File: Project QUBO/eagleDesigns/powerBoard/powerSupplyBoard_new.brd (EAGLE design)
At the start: 152.4 x 101.6 mm, 146 parts

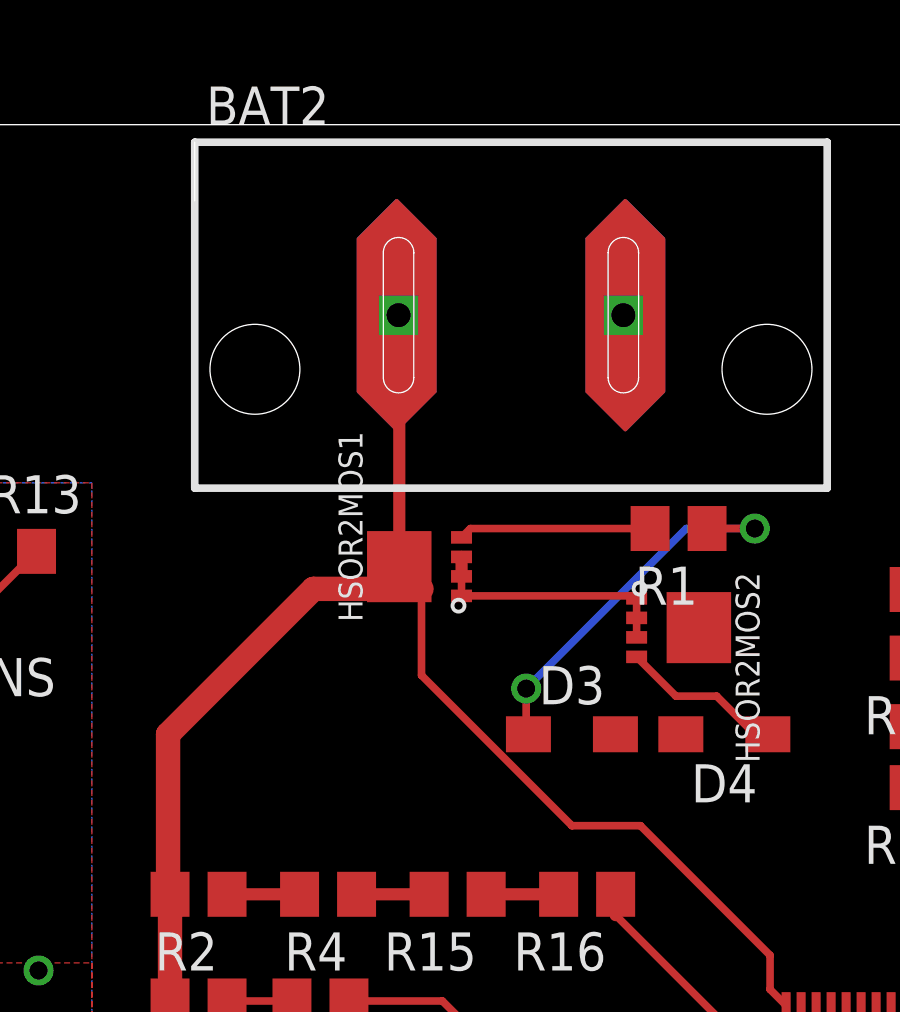
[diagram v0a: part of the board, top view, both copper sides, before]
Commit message: 
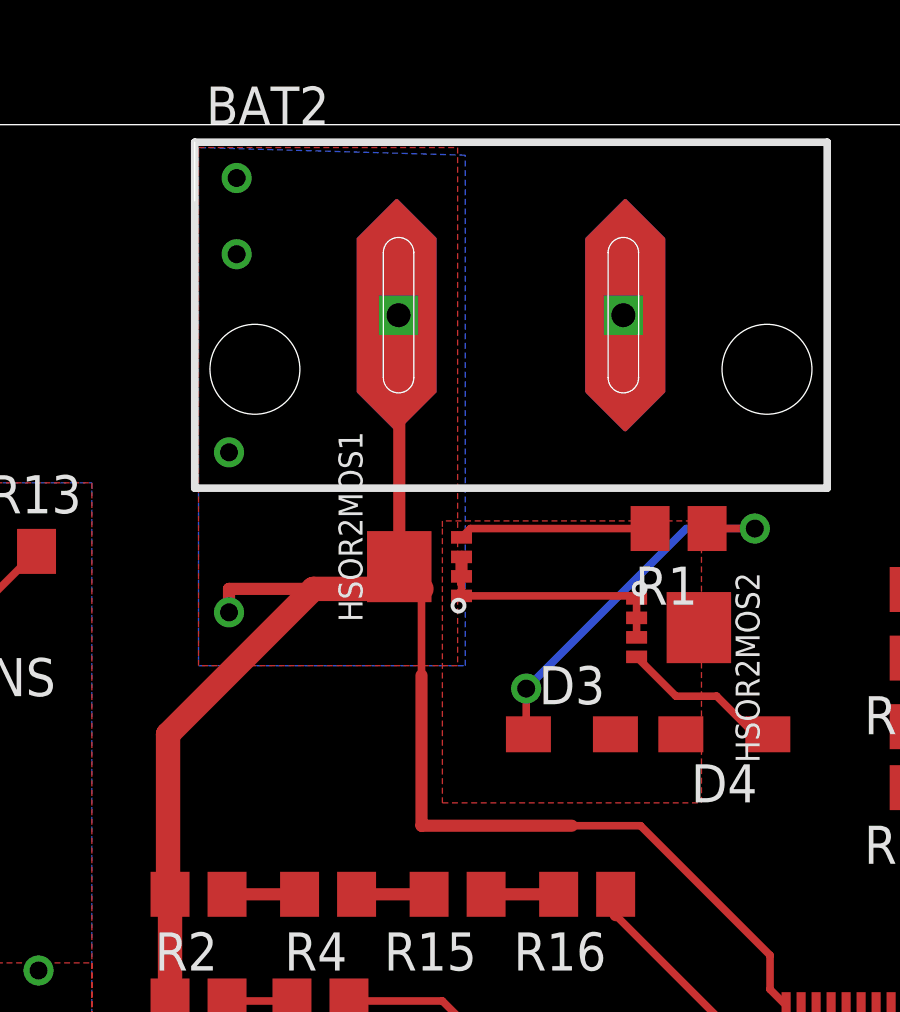
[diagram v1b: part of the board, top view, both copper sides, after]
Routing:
- net BAT2: track 52.9 -> 59.4 mm, vias 0 -> 4
- added copper zone on layer 1, net BAT2
- added copper zone on layer 16, net BAT2
- added copper zone on layer 1, net N$27
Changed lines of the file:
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@@
 <wire x1="67.31" y1="81.28" x2="67.31" y2="76.012" width="0.8128" layer="1"/>
 <wire x1="67.31" y1="76.012" x2="67.376" y2="75.946" width="0.254" layer="1"/>
-<wire x1="75.758" y1="86.127" x2="75.758" y2="83.246" width="0.254" layer="1"/>
-<wire x1="75.758" y1="83.246" x2="80.772" y2="78.232" width="0.254" layer="1"/>
-<wire x1="80.772" y1="78.232" x2="83.058" y2="78.232" width="0.254" layer="1"/>
+<wire x1="75.758" y1="83.246" x2="75.758" y2="86.127" width="0.254" layer="1"/>
+<wire x1="83.058" y1="78.232" x2="80.772" y2="78.232" width="0.254" layer="1"/>
 <wire x1="83.058" y1="78.232" x2="87.376" y2="73.914" width="0.254" layer="1"/>
 <wire x1="87.376" y1="73.914" x2="87.376" y2="72.776" width="0.254" layer="1"/>
 <wire x1="87.376" y1="72.776" x2="87.912" y2="72.24" width="0.254" layer="1"/>
+<wire x1="80.772" y1="78.232" x2="75.758" y2="78.232" width="0.4064" layer="1"/>
+<wire x1="75.758" y1="78.232" x2="75.758" y2="83.246" width="0.4064" layer="1"/>
+<polygon width="0.4064" layer="1">
+<vertex x="68.326" y="100.838"/>
+<vertex x="76.962" y="100.838"/>
+<vertex x="76.962" y="83.566"/>
+<vertex x="68.326" y="83.566"/>
+<vertex x="68.326" y="100.584"/>
+</polygon>
+<polygon width="0.4064" layer="16">
+<vertex x="68.326" y="100.838"/>
+<vertex x="68.326" y="83.566"/>
+<vertex x="77.216" y="83.566"/>
+<vertex x="77.216" y="100.584"/>
+<vertex x="68.326" y="100.838"/>
+</polygon>
+<via x="69.596" y="99.822" extent="1-16" drill="0.6"/>
+<via x="69.596" y="97.282" extent="1-16" drill="0.6"/>
+<via x="69.342" y="90.678" extent="1-16" drill="0.6"/>
+<via x="69.342" y="85.344" extent="1-16" drill="0.6"/>
+<wire x1="72.157" y1="86.127" x2="69.342" y2="86.127" width="0.4064" layer="1"/>
+<wire x1="69.342" y1="86.127" x2="69.342" y2="85.344" width="0.4064" layer="1"/>
 <wire x1="87.912" y1="72.24" x2="146.37" y2="64.77" width="0" layer="19" extent="1-1"/>
 </signal>
@@
 <wire x1="77.092" y1="85.893" x2="82.846" y2="85.893" width="0.254" layer="1"/>
 <wire x1="82.846" y1="85.893" x2="82.928" y2="85.811" width="0.254" layer="1"/>
-<wire x1="82.222" y1="81.28" x2="84.402" y2="81.28" width="0" layer="19" extent="1-1"/>
-<wire x1="82.928" y1="84.511" x2="82.222" y2="81.28" width="0" layer="19" extent="1-1"/>
-<wire x1="89.412" y1="72.24" x2="84.402" y2="81.28" width="0" layer="19" extent="1-1"/>
+<polygon width="0.4064" layer="1" rank="2">
+<vertex x="76.454" y="88.138"/>
+<vertex x="76.454" y="78.994"/>
+<vertex x="85.09" y="78.994"/>
+<vertex x="85.09" y="88.392"/>
+<vertex x="76.454" y="88.392"/>
+</polygon>
+<wire x1="84.402" y1="81.28" x2="89.412" y2="72.24" width="0" layer="19" extent="1-1"/>
 </signal>
 <signal name="N$29">

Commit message: 
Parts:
- moved BAT2CS 25.5 mm to (104.6, 65.5), turned to 270 degrees
- moved R17 0.25 mm to (87.1, 61.0)
- moved R22 0.25 mm to (93.0, 79.2), turned to 0 degrees
- turned R20 to 180 degrees
- turned R21 to 0 degrees
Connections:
- new net UWEEN: DVL_12VREG.ONOFF, IOEXPANDER.9
- net BAT1: now also BAT1.P$2
- net BAT2: now also BAT2.P$2
- net BAT3: now also SHORE.P$2
- net GND: no longer BAT1.P$2, BAT2.P$2, SHORE.P$2
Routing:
- net BAT2HSOROUT: track 0.00 -> 25.4 mm, vias 0 -> 2
- net N$5: track 0.00 -> 22.2 mm
- net N$23: track 0.00 -> 15.1 mm
- net N$2: track 13.0 -> 27.2 mm
- net N$27: track 8.47 -> 19.6 mm
- net N$4: track 5.44 -> 15.6 mm
- net N$34: track 0.00 -> 3.38 mm
- net N$22: track 0.00 -> 2.29 mm
- net GND: track 167.5 -> 165.8 mm
- net BAT3HSOROUT: track 55.7 -> 55.9 mm, vias 4 -> 9

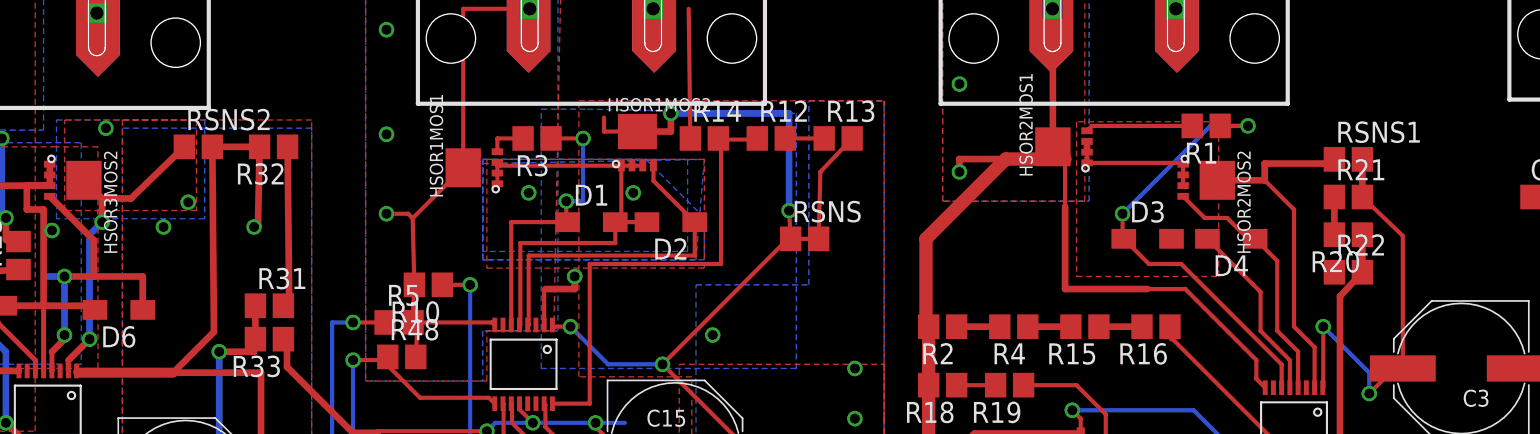
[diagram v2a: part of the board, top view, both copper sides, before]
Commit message: got rid of sense resistor on psb
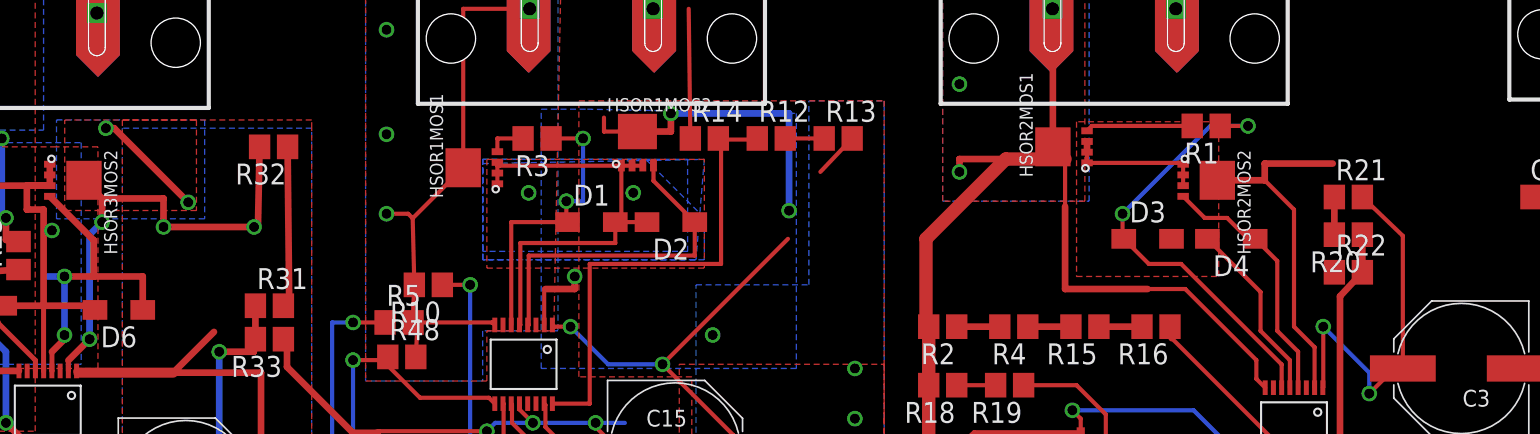
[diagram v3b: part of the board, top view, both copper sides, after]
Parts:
- removed RSNS, RSNS1, RSNS2: 2 mO, resistor:R0805
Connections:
- removed net N$1: BAT1HSOR.SENSE, HSOR1MOS2.DRAIN, RSNS.1
- removed net N$43: BAT3HSOR.SENSE, HSOR3MOS2.DRAIN, RSNS2.1
- removed net N$5: BAT2HSOR.SENSE, HSOR2MOS2.DRAIN, RSNS1.1
- net BAT1HSOROUT: now also BAT1HSOR.SENSE, HSOR1MOS2.DRAIN; no longer RSNS.2
- net BAT2HSOROUT: now also BAT2HSOR.SENSE, HSOR2MOS2.DRAIN; no longer RSNS1.2
- net BAT3HSOROUT: now also BAT3HSOR.SENSE, HSOR3MOS2.DRAIN; no longer RSNS2.2
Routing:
- net N$1: track 25.7 -> 0.00 mm, vias 3 -> 0
- net N$5: track 22.2 -> 0.00 mm
- net BAT2HSOROUT: track 25.4 -> 44.9 mm
- net BAT1HSOROUT: track 44.3 -> 62.4 mm, vias 6 -> 9
- net N$43: track 19.2 -> 6.86 mm, vias 4 -> 2
- net BAT3HSOROUT: track 55.9 -> 65.7 mm, vias 9 -> 11

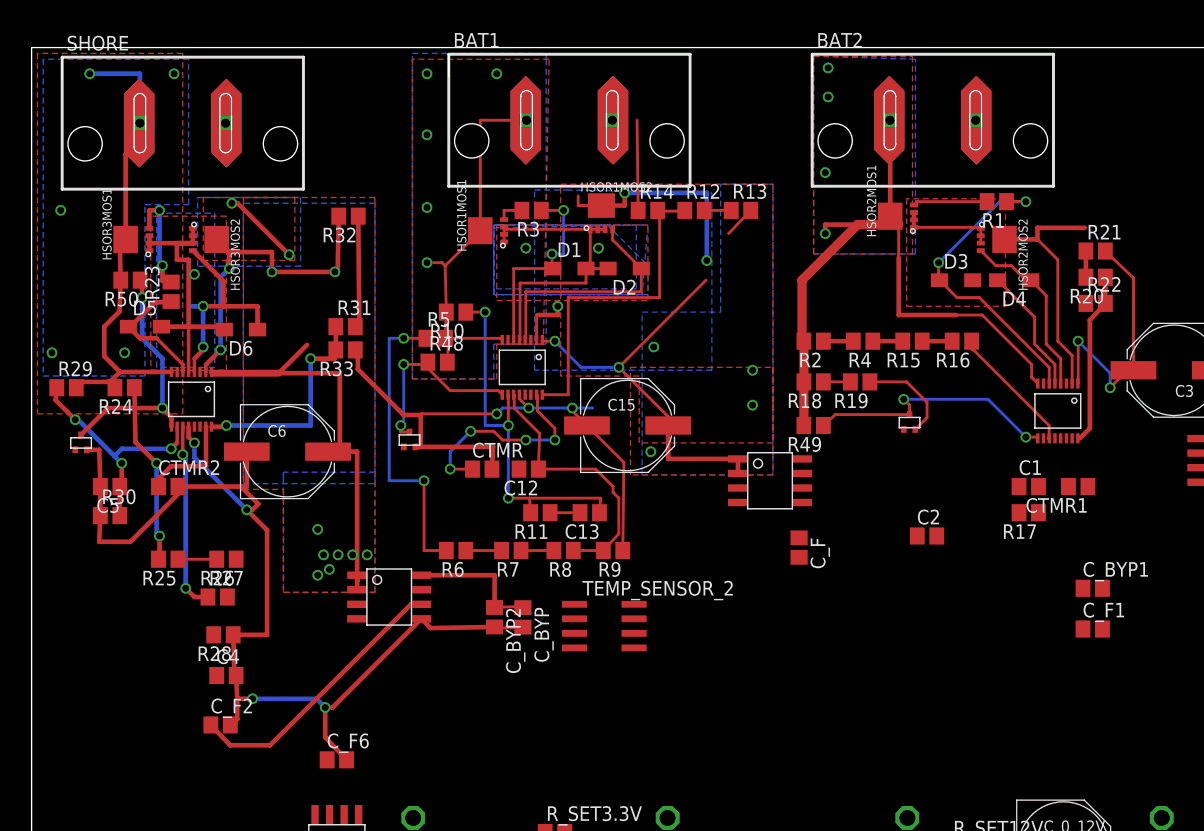
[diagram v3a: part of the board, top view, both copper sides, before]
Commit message: 
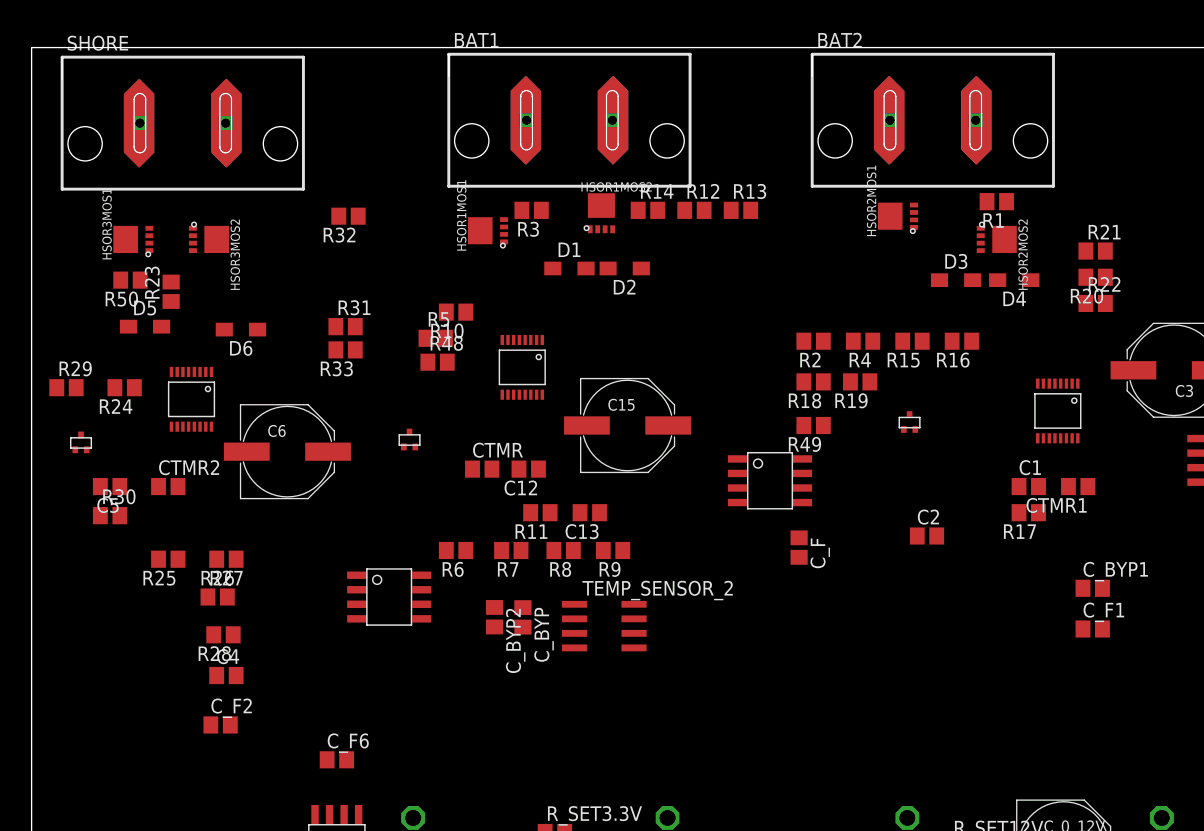
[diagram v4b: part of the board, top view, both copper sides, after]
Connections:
- removed net GND: 12VCS.P$5, 12VREG.P$1, 12VREG.P$2, 16VCS.P$5, 16V_CON.P$1, 3.3VCS.P$5, 3.3VREG.P$1, 3.3VREG.P$2, 5VCS.P$5, 5VREG.AGND1, 5VREG.AGND2, 5VREG.PGND, 5VREG.SYNC, ADC.COM, ADC.F0, ADC.GND0, ADC.GND1, ADC.GND2, ADC.GND3, ADC.GND4, ADC.GND5, ADC.GND6, ADC.REF-, BAT1CS.P$5, BAT1HSOR.GND, BAT2CS.P$5, BAT2HSOR.GND, BAT3CS.P$5, BAT3HSOR.GND, C1.2, C12.2, C15.-, C2.2, C3.-, C4.2, C5.2, C6.-, CTMR.2, CTMR1.2, CTMR2.2, C_0_12V.-, C_0_3.3V.-, C_1_12V.2, C_1_3.3V.2, C_BYP.2, C_BYP1.2, C_BYP2.2, C_BYP3.2, C_BYP4.2, C_BYP5.2, C_BYP6.2, C_BYP7.2, C_F.2, C_F1.2, C_F2.2, C_F3.2, C_F4.2, C_F5.2, C_F6.2, C_IN_5V.2, C_OUT_5V.-, DVL_12VREG.-VIN, HIGHSIDEMOS1.S, HIGHSIDEMOS2.S, HIGHSIDEMOS3.S, IOEXPANDER.12, JP1.12, JP1.15, JP1.18, JP1.24, JP1.33, JP1.34, JP1.37, JP1.39, JP1.4, JP1.40, JP1.44, JP1.64, R14.1, R17.1, R19.1, R22.1, R28.1, R30.1, R33.1, R35.1, R37.1, R39.1, R41.1, R43.1, R45.1, R47.1, R9.1, REN_B.1, REN_B.2, REN_H.1, REN_T.2, RFBB.2, R_LOAD.1, R_SET12V.1, R_SET3.3V.1, TEMP_SENSOR_1.4, TEMP_SENSOR_2.4, U$10.GND, U$14.S, U$15.S, U$16.GND, U$17.VCC, U$18.GND, U$5.A, U$5.C, U$6.GND, U$9.GND
- removed net N$100: JP1.36
- removed net SCL1: ADC.SCL, IOEXPANDER.22, JP1.10
- removed net SDA1: ADC.SDA, IOEXPANDER.23, JP1.9
- new net AGND: 12VCS.P$5, 12VREG.P$1, 12VREG.P$2, 16VCS.P$5, 16V_CON.P$1, 3.3VCS.P$5, 3.3VREG.P$1, 3.3VREG.P$2, 5VCS.P$5, 5VREG.AGND1, 5VREG.AGND2, 5VREG.PGND, 5VREG.SYNC, ADC.F0, BAT1CS.P$5, BAT1HSOR.GND, BAT2CS.P$5, BAT2HSOR.GND, BAT3CS.P$5, BAT3HSOR.GND, C1.2, C12.2, C15.-, C2.2, C3.-, C4.2, C5.2, C6.-, CTMR.2, CTMR1.2, CTMR2.2, C_0_12V.-, C_0_3.3V.-, C_1_12V.2, C_1_3.3V.2, C_BYP.2, C_BYP1.2, C_BYP2.2, C_BYP3.2, C_BYP4.2, C_BYP5.2, C_BYP6.2, C_BYP7.2, C_F.2, C_F1.2, C_F2.2, C_F3.2, C_F4.2, C_F5.2, C_F6.2, C_IN_5V.2, C_OUT_5V.-, DVL_12VREG.-VIN, HIGHSIDEMOS1.S, HIGHSIDEMOS2.S, HIGHSIDEMOS3.S, JP1.19, JP1.20, JP1.39, JP1.40, JP1.59, JP1.60, JP1.79, JP1.80, R14.1, R17.1, R19.1, R22.1, R28.1, R30.1, R33.1, R35.1, R37.1, R39.1, R41.1, R43.1, R45.1, R47.1, R9.1, REN_B.1, REN_B.2, REN_H.1, REN_T.2, RFBB.2, R_LOAD.1, R_SET12V.1, R_SET3.3V.1, TEMP_SENSOR_1.4, TEMP_SENSOR_2.4, U$10.GND, U$14.S, U$15.S, U$16.GND, U$17.VCC, U$18.GND, U$5.A, U$5.C, U$6.GND, U$9.GND
- new net DGND: ADC.COM, ADC.GND0, ADC.GND1, ADC.GND2, ADC.GND3, ADC.GND4, ADC.GND5, ADC.GND6, ADC.REF-, IOEXPANDER.12, JP1.1, JP1.15, JP1.21, JP1.25, JP1.32, JP1.35, JP1.47, JP1.55, JP1.63, JP1.75
- new net INT_SCL: ADC.SCL, IOEXPANDER.22, JP1.66
- new net INT_SDA: ADC.SDA, IOEXPANDER.23, JP1.65
- net 12V: now also JP1.16, JP1.36, JP1.56, JP1.76; no longer JP1.1, JP1.21, JP1.41, JP1.61
- net 3.3V: now also JP1.18, JP1.38, JP1.58, JP1.78; no longer JP1.23, JP1.3, JP1.43, JP1.63
- net 5V: now also JP1.17, JP1.37, JP1.57, JP1.77; no longer JP1.2, JP1.22, JP1.42, JP1.62
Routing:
- net GND: track 165.8 -> 0.00 mm, vias 7 -> 0
- net BAT3HSOROUT: track 65.7 -> 0.00 mm, vias 11 -> 0
- net BAT1HSOROUT: track 62.4 -> 0.00 mm, vias 9 -> 0
- net BAT2: track 59.5 -> 0.00 mm, vias 4 -> 0
- net BAT2HSOROUT: track 44.9 -> 0.00 mm, vias 2 -> 0
- net BAT3: track 42.6 -> 0.00 mm, vias 5 -> 0
- net BAT1: track 33.3 -> 0.00 mm, vias 5 -> 0
- net N$15: track 33.3 -> 0.00 mm, vias 3 -> 0
- net N$17: track 28.9 -> 0.00 mm
- net N$68: track 27.9 -> 0.00 mm, vias 2 -> 0
- net N$2: track 27.2 -> 0.00 mm, vias 2 -> 0
- net N$8: track 26.7 -> 0.00 mm, vias 2 -> 0
- net N$11: track 25.7 -> 0.00 mm, vias 1 -> 0
- net N$45: track 24.3 -> 0.00 mm
- net N$14: track 23.5 -> 0.00 mm
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- removed copper zone on layer 1, net BAT1
- removed copper zone on layer 16, net BAT1
- removed copper zone on layer 1, net BAT1HSOROUT
- removed copper zone on layer 16, net BAT1HSOROUT
- removed copper zone on layer 1, net BAT2
- removed copper zone on layer 16, net BAT2
- removed copper zone on layer 1, net BAT3
- removed copper zone on layer 16, net BAT3
- removed copper zone on layer 1, net BAT3HSOROUT
- removed copper zone on layer 16, net BAT3HSOROUT
- removed copper zone on layer 16, net N$1
- removed copper zone on layer 1, net N$11
- removed copper zone on layer 16, net N$11
- removed copper zone on layer 1, net N$27
- removed copper zone on layer 1, net N$43
- removed copper zone on layer 16, net N$43
- removed copper zone on layer 1, net N$68
- removed copper zone on layer 16, net N$68
